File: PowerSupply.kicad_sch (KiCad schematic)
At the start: 35 parts

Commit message: added connector part
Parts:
- added TP? (x5): (no value), symbol Connector:TestPoint
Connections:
- net +3.3VA: now also TP?.1
- net +3V3: now also TP?.1
- net GNDREF: now also TP?.1
- net VBat: now also TP?.1
- net Vbat: now also TP?.1
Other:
- moved on the sheet: C?

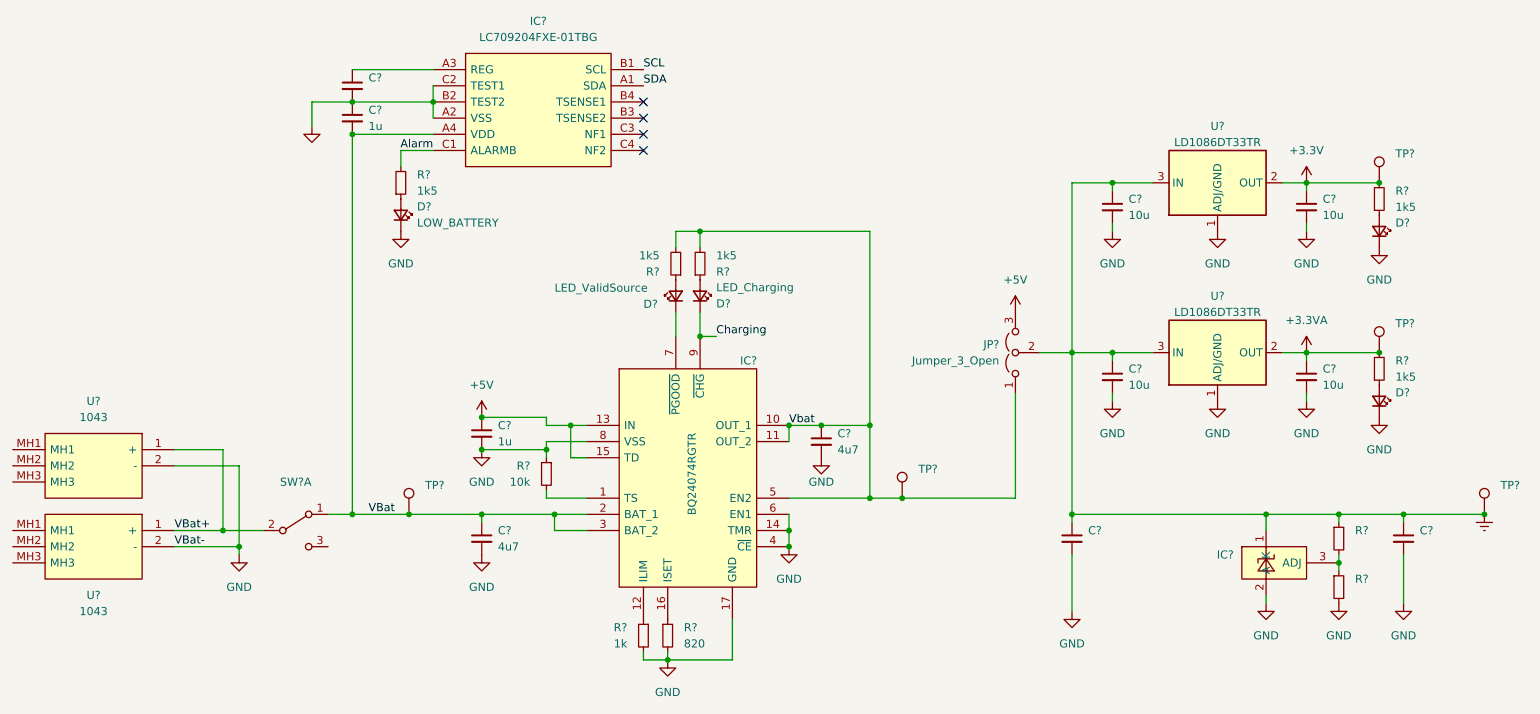
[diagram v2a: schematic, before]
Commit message: resolve DRC on schematic
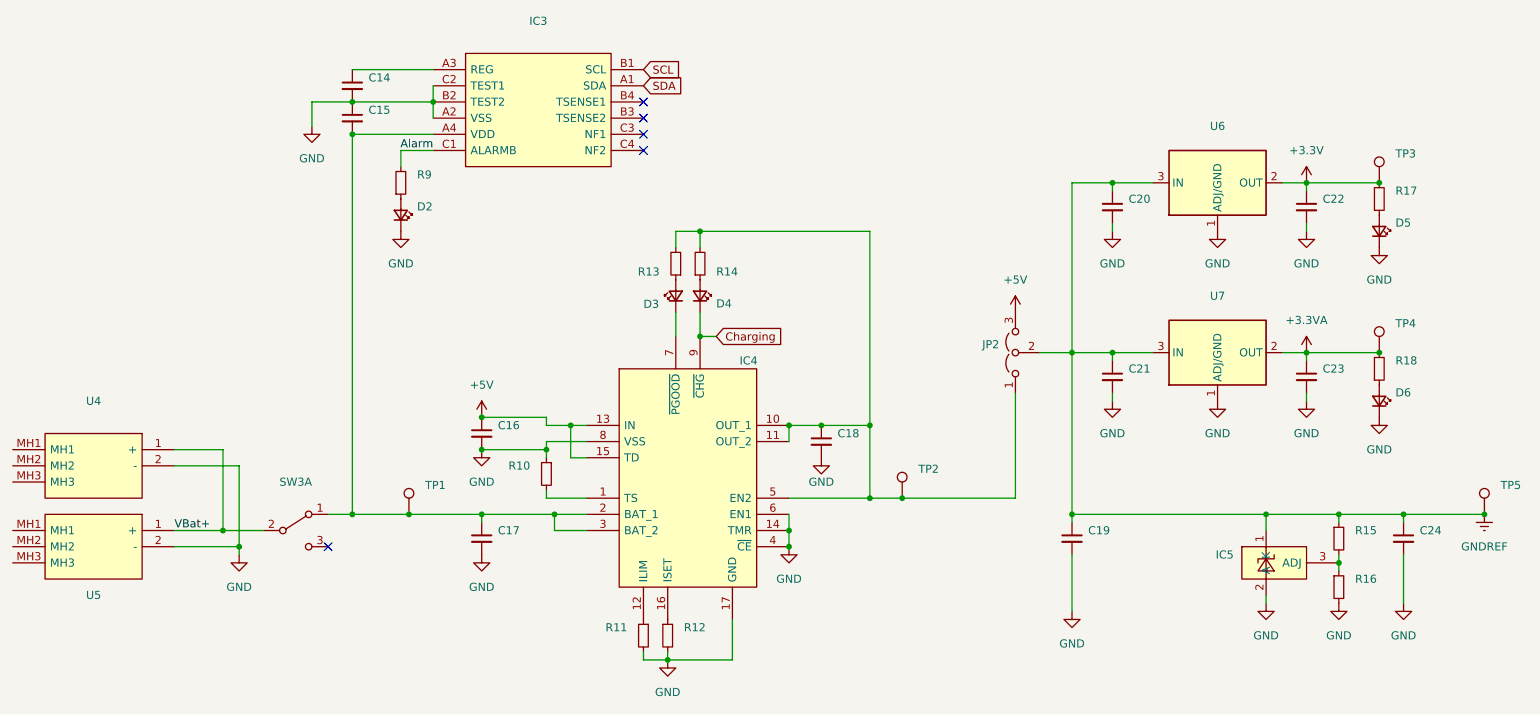
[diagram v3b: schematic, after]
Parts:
- C14, C24: renamed from C?; footprint Capacitor_SMD:C_0805_2012Metric_Pad1.18x1.45mm_HandSolder -> (none)
- C15, C16: renamed from C?; value 1u -> (none); footprint Capacitor_SMD:C_0805_2012Metric_Pad1.18x1.45mm_HandSolder -> (none)
- C17, C18: renamed from C?; value 4u7 -> (none); footprint Capacitor_SMD:C_0805_2012Metric_Pad1.18x1.45mm_HandSolder -> (none)
- C20, C21, C22, C23: renamed from C?; value 10u -> (none); footprint Capacitor_SMD:C_0805_2012Metric_Pad1.18x1.45mm_HandSolder -> (none)
- D2: renamed from D?; value LOW_BATTERY -> (none); footprint LED_SMD:LED_0805_2012Metric_Pad1.15x1.40mm_HandSolder -> (none)
- D3: renamed from D?; value LED_ValidSource -> (none); footprint LED_SMD:LED_0805_2012Metric_Pad1.15x1.40mm_HandSolder -> (none)
- D4: renamed from D?; value LED_Charging -> (none); footprint LED_SMD:LED_0805_2012Metric_Pad1.15x1.40mm_HandSolder -> (none)
- D5, D6: renamed from D?; footprint LED_SMD:LED_0805_2012Metric_Pad1.15x1.40mm_HandSolder -> (none)
- IC3: renamed from IC?; value LC709204FXE-01TBG -> (none); footprint BGA12C40P4X3_191X148X51 -> (none)
- IC4: renamed from IC?; value BQ24074RGTR -> (none); footprint project_library:BQ24074RGTR -> (none)
- JP2: renamed from JP?; value Jumper_3_Open -> (none); footprint Connector_PinHeader_2.54mm:PinHeader_1x03_P2.54mm_Vertical -> (none)
- R10: renamed from R?; value 10k -> (none); footprint Resistor_SMD:R_0805_2012Metric_Pad1.20x1.40mm_HandSolder -> (none)
- R11: renamed from R?; value 1k -> (none); footprint Resistor_SMD:R_0805_2012Metric_Pad1.20x1.40mm_HandSolder -> (none)
- R12: renamed from R?; value 820 -> (none); footprint Resistor_SMD:R_0805_2012Metric_Pad1.20x1.40mm_HandSolder -> (none)
- R13, R14, R17, R18, R9: renamed from R?; value 1k5 -> (none); footprint Resistor_SMD:R_0805_2012Metric_Pad1.20x1.40mm_HandSolder -> (none)
- R15, R16: renamed from R?; footprint Resistor_SMD:R_0805_2012Metric_Pad1.20x1.40mm_HandSolder -> (none)
- U4, U5: renamed from U?; value 1043 -> (none); footprint project_library:1043 -> (none)
- U6, U7: renamed from U?; value LD1086DT33TR -> (none); footprint Package_TO_SOT_SMD:TO-252-2 -> (none)
- gave numbers to parts that had none: 8
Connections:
- net VBat: no longer names the net of C15.2, C17.1, IC3.A4 (VDD), IC4.2 (BAT_1), IC4.3 (BAT_2), SW3.1 (A), TP1.1
- net Vbat: no longer names the net of C18.1, IC4.10 (OUT_1), IC4.11 (OUT_2), IC4.5 (EN2), JP2.1 (A), R13.2, R14.2, TP2.1
- no-connect marks 4 -> 5
